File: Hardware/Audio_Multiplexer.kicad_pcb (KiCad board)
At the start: 2 copper layers, 147 x 40 mm, 14 parts, among them J1 FC68131, J2 FC68131, J3 FC68131, J4 FC68131, J5 FC68131, J6 FC68131, J7 FC68131, SW1 7301SYZQE, SW2 7301SYZQE, SW3 7301SYZQE

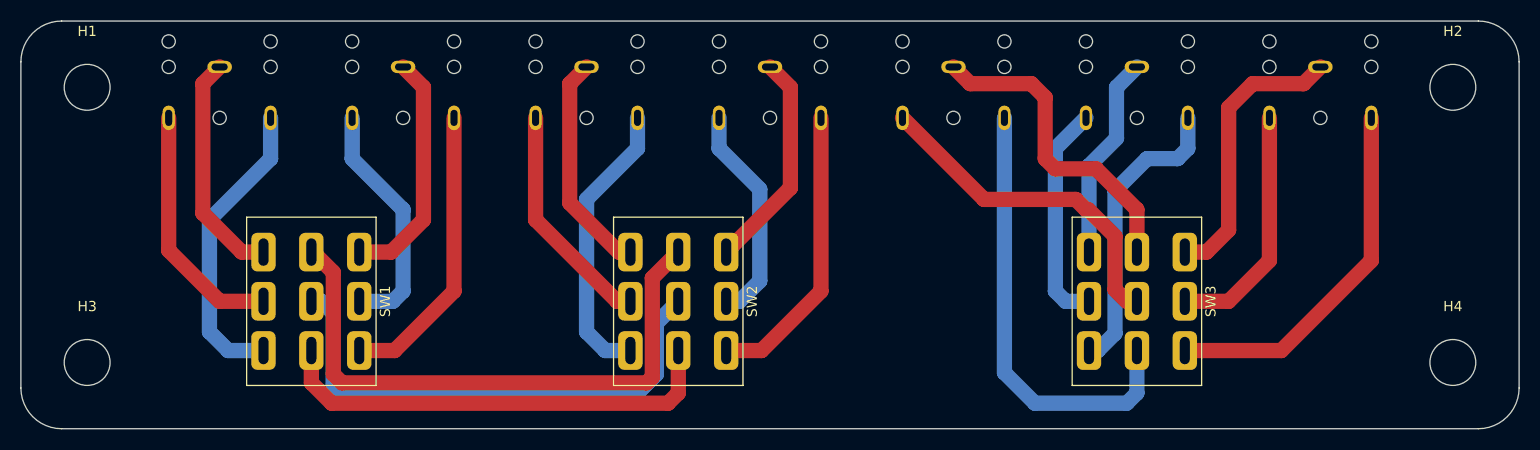
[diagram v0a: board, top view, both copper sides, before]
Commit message: Added copper planes to PCB top and bottom layers in order to decrease the amount of copper to remove. This simplifies the PCB manufacturing process.
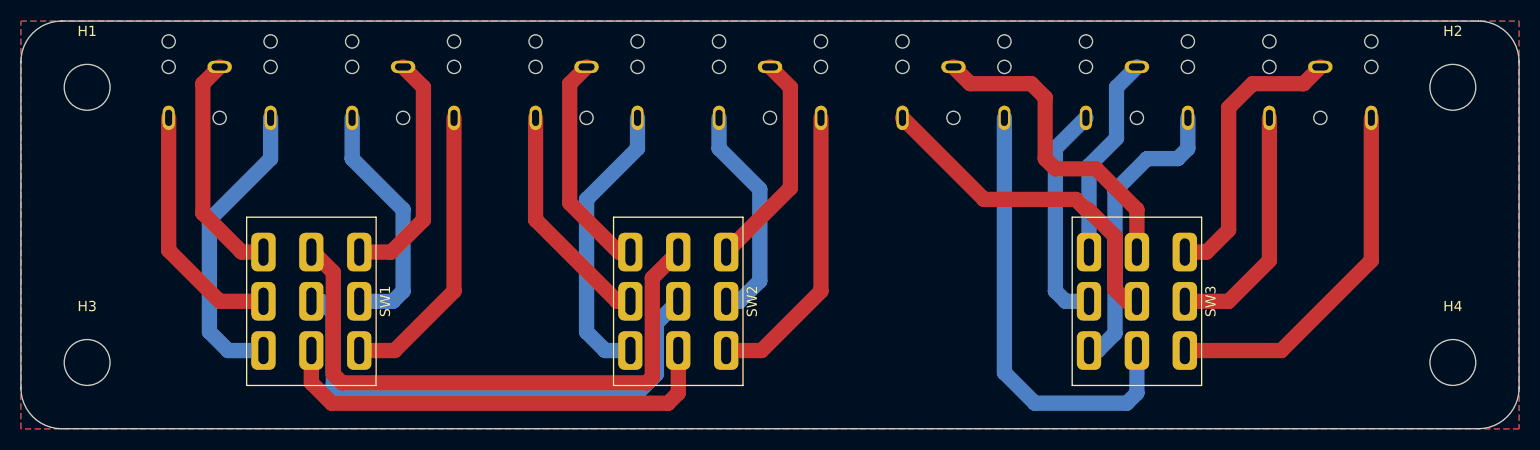
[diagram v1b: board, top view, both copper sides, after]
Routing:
- added copper zone on B.Cu, net (none)
- added copper zone on F.Cu, net (none)
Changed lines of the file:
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@@
   (segment (start 63.15 88.15) (end 61.17 86.17) (width 1.5) (layer "F.Cu") (net 24))
   (segment (start 94.45 98.45) (end 93.9 99) (width 1.5) (layer "F.Cu") (net 24))
+  (zone (net 0) (net_name "") (layers F&B.Cu) (hatch edge 0.508)
+    (connect_pads (clearance 0.508))
+    (min_thickness 0.254) (filled_areas_thickness no)
+    (fill yes (thermal_gap 0.508) (thermal_bridge_width 0.508))
+    (polygon
+      (pts
+        (xy 179.5 103.5)
+        (xy 32.5 103.5)
+        (xy 32.5 63.5)
+        (xy 179.5 63.5)
+      )
+    )
+  )
 )

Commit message: Added jack connectors label silkscreen texts to the PCB. Also added the design date.
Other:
- board text added: "15/07/2022"
- board text added: "AUDIO IN 1"
- board text added: "AUDIO IN 2"
- board text added: "AUDIO OUT 1"
- board text added: "AUDIO OUT 2"
- board text added: "MIC IN"
- board text added: "MIC OUT 1"
- board text added: "MIC OUT 2"
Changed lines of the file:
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@@
   (gr_line (start 175.5 63.5) (end 36.5 63.5) (layer "Edge.Cuts") (width 0.1))
   (gr_arc (start 36.5 103.5) (mid 33.671573 102.328427) (end 32.5 99.5) (layer "Edge.Cuts") (width 0.1))
+  (gr_text "AUDIO OUT 1" (at 88 64.5 180) (layer "F.SilkS")
+    (effects (font (size 1 1) (thickness 0.15)))
+  )
+  (gr_text "AUDIO IN 1" (at 52 64.5 180) (layer "F.SilkS")
+    (effects (font (size 1 1) (thickness 0.15)))
+  )
+  (gr_text "MIC IN" (at 124 64.5 180) (layer "F.SilkS")
+    (effects (font (size 1 1) (thickness 0.15)))
+  )
+  (gr_text "AUDIO OUT 2" (at 106 64.5 180) (layer "F.SilkS")
+    (effects (font (size 1 1) (thickness 0.15)))
+  )
+  (gr_text "MIC OUT 1" (at 142 64.5 180) (layer "F.SilkS")
+    (effects (font (size 1 1) (thickness 0.15)))
+  )
+  (gr_text "MIC OUT 2" (at 160 64.5 180) (layer "F.SilkS")
+    (effects (font (size 1 1) (thickness 0.15)))
+  )
+  (gr_text "AUDIO IN 2" (at 70 64.5 180) (layer "F.SilkS")
+    (effects (font (size 1 1) (thickness 0.15)))
+  )
+  (gr_text "15/07/2022" (at 158.5 100) (layer "F.Mask")
+    (effects (font (size 1 1) (thickness 0.15)))
+  )
   (segment (start 54.17 86.17) (end 56.3 86.17) (width 1.5) (layer "F.Cu") (net 1))
   (segment (start 50.349999 82.349999) (end 54.17 86.17) (width 1.5) (layer "F.Cu") (net 1))
